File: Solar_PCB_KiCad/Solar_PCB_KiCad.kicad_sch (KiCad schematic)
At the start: 1 part, among them U1 LT3652EMSE

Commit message: Updated Schematic
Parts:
- added C1, C2: C, symbol Device:C
- added D1, D2: LED, symbol Device:LED
- added D3, D4: D_Schottky, symbol Device:D_Schottky
- added J1, J2: Screw_Terminal_01x02, symbol Connector:Screw_Terminal_01x02
- added L1: L, symbol Device:L
- added R1, R2, R3, R4, R5, R6: R, symbol Device:R
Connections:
- net at U1.1 (V_{IN}): now also U1.2 (V_{IN_REG}), U1.3 (~{SHDN}), J1.1 (Pin_1), R1.1, R2.1
- net at U1.10 (SENSE): now also L1.2, R6.2
- net at U1.11 (BOOST): now also C2.2, D3.1 (K)
- net at U1.12 (SW): now also C2.1, D4.1 (K), L1.1
- net GND: now reaches U1.13 (GND)
- net GND: now also U1.6 (TIMER), C1.2, D4.2 (A), J1.2 (Pin_2), R4.1
- net at U1.4 (~{CHRG}): now also D1.1 (K)
- net at U1.5 (~{FAULT}): now also D2.1 (K)
- net at U1.7 (V_{FB}): now also R3.1
- net at U1.9 (BAT): now also C1.1, D3.2 (A), J2.1 (Pin_1), R5.1, R6.1
- new net: R3.2, R4.2, R5.2
- new net: D2.2 (A), R2.2
- new net: D1.2 (A), R1.2

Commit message: Updated schematic & PCB
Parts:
- C1, C2: footprint (none) -> Capacitor_SMD:C_0603_1608Metric
- D1, D2: footprint (none) -> LED_SMD:LED_0603_1608Metric
- D3, D4: footprint (none) -> Diode_SMD:D_0603_1608Metric
- J1, J2: footprint (none) -> TerminalBlock_Phoenix:TerminalBlock_Phoenix_MKDS-1,5-2-5.08_1x02_P5.08mm_Horizontal
- L1: footprint (none) -> Inductor_SMD:L_0603_1608Metric
- R1, R2, R3, R4, R5, R6: footprint (none) -> Resistor_SMD:R_0603_1608Metric
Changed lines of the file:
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@@
 			)
 		)
-		(property "Footprint" ""
+		(property "Footprint" "Diode_SMD:D_0603_1608Metric"
 			(at 175.26 80.01 0)
 			(effects
@@
 			)
 		)
-		(property "Footprint" ""
+		(property "Footprint" "Resistor_SMD:R_0603_1608Metric"
 			(at 198.12 90.678 90)
 			(effects
@@
 			)
 		)
-		(property "Footprint" ""
+		(property "Footprint" "Inductor_SMD:L_0603_1608Metric"
 			(at 186.69 88.9 0)
 			(effects
@@
 			)
 		)
-		(property "Footprint" ""
+		(property "Footprint" "Resistor_SMD:R_0603_1608Metric"
 			(at 179.832 113.03 90)
 			(effects
@@
 			)
 		)
-		(property "Footprint" ""
+		(property "Footprint" "TerminalBlock_Phoenix:TerminalBlock_Phoenix_MKDS-1,5-2-5.08_1x02_P5.08mm_Horizontal"
 			(at 102.87 77.47 0)
 			(effects
@@
 			)
 		)
-		(property "Footprint" ""
+		(property "Footprint" "Resistor_SMD:R_0603_1608Metric"
 			(at 127 103.632 90)
 			(effects
@@
 			)
 		)
-		(property "Footprint" ""
+		(property "Footprint" "Capacitor_SMD:C_0603_1608Metric"
 			(at 176.2252 96.52 0)
 			(effects
@@
 			)
 		)
-		(property "Footprint" ""
+		(property "Footprint" "LED_SMD:LED_0603_1608Metric"
 			(at 135.89 105.41 0)
 			(effects
@@
 			)
 		)
-		(property "Footprint" ""
+		(property "Footprint" "Capacitor_SMD:C_0603_1608Metric"
 			(at 199.0852 116.84 0)
 			(effects
@@
 			)
 		)
-		(property "Footprint" ""
+		(property "Footprint" "Resistor_SMD:R_0603_1608Metric"
 			(at 187.96 108.458 90)
 			(effects
@@
 			)
 		)
-		(property "Footprint" ""
+		(property "Footprint" "LED_SMD:LED_0603_1608Metric"
 			(at 135.89 100.33 0)
 			(effects
@@
 			)
 		)
-		(property "Footprint" ""
+		(property "Footprint" "TerminalBlock_Phoenix:TerminalBlock_Phoenix_MKDS-1,5-2-5.08_1x02_P5.08mm_Horizontal"
 			(at 227.33 88.9 0)
 			(effects
@@
 			)
 		)
-		(property "Footprint" ""
+		(property "Footprint" "Diode_SMD:D_0603_1608Metric"
 			(at 186.69 96.52 0)
 			(effects
@@
 			)
 		)
-		(property "Footprint" ""
+		(property "Footprint" "Resistor_SMD:R_0603_1608Metric"
 			(at 175.26 104.902 90)
 			(effects
@@
 			)
 		)
-		(property "Footprint" ""
+		(property "Footprint" "Resistor_SMD:R_0603_1608Metric"
 			(at 127 102.108 90)
 			(effects

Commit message: Updated Schematics
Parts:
- added C3: 10u, Capacitor_SMD:C_0603_1608Metric, symbol Device:C
- C1: value C -> 10u
- C2: value C -> 1u
- D1: value LED -> GREEN LED
- D2: value LED -> RED LED
- R1, R2: value R -> 2k
- R3: value R -> 67.2k
- R4: value R -> 330k
- R5: value R -> 410k
- R6: value R -> 0.2
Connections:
- net GND: now also C3.2
- net at J1.1 (Pin_1), R1.1, R2.1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: now also C3.1
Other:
- title: (none) -> Solar_PCB
- moved on the sheet: J1

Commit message: Updated simulation
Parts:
- added D5: D_Schottky, Diode_SMD:D_0603_1608Metric, symbol Device:D_Schottky
- L1: value L -> 18.91uH; footprint Inductor_SMD:L_0603_1608Metric -> Inductor_THT:L_Radial_D7.8mm_P5.00mm_Fastron_07HCP
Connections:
- net GND: now also J2.2 (Pin_2)
- net at C3.1, R1.1, R2.1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: now also D5.1 (K); no longer J1.1 (Pin_1)
- new net: D5.2 (A), J1.1 (Pin_1)
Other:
- moved on the sheet: C2, C3, D1, D2, D4, J1, J2, L1, R1, R2, R6

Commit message: Updated BOM
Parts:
- R1, R2: value 2k -> 100
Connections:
- net at C3.1, D5.1 (K), U1.1 (V_{IN})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: now also D1.2 (A), D2.2 (A); no longer R1.1, R2.1
- net at R2.2: now also U1.5 (~{FAULT}); no longer D2.2 (A)
- net at D2.1 (K): now also R2.1; no longer U1.5 (~{FAULT})
- net at D1.1 (K): now also R1.1; no longer U1.4 (~{CHRG})
- net at R1.2: now also U1.4 (~{CHRG}); no longer D1.2 (A)
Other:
- moved on the sheet: D1, D2, R1, R2
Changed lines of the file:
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@@
 		)
 	)
-	(text_box "Solar Panel Input\n12V 300mA 4W Max"
+	(text_box "Solar Panel Input\n12V 350mA 4W Max"
 		(exclude_from_sim no)
 		(at 45.72 88.9 0)
@@
 		)
 	)
-	(text_box "Status pins can sink up to 10mA\n\nI = 12V/2k = 6mA"
+	(text_box "Status pins can sink up to 10mA\n\nI = (12V-2V)/100 = 100mA"
 		(exclude_from_sim no)
 		(at 86.36 101.6 0)
@@
 	(symbol
 		(lib_id "Device:R")
-		(at 123.19 105.41 90)
+		(at 132.08 105.41 90)
 		(mirror x)
 		(unit 1)
@@
 		(dnp no)
 		(property "Reference" "R2"
-			(at 123.19 111.76 90)
-			(effects
-				(font
-					(size 1.27 1.27)
-				)
-			)
-		)
-		(property "Value" "2k"
-			(at 123.19 109.22 90)
+			(at 132.08 111.76 90)
+			(effects
+				(font
+					(size 1.27 1.27)
+				)
+			)
+		)
+		(property "Value" "100"
+			(at 132.08 109.22 90)
 			(effects
 				(font
@@
 		)
 		(property "Footprint" "Resistor_SMD:R_0603_1608Metric"
-			(at 123.19 103.632 90)
+			(at 132.08 103.632 90)
 			(effects
 				(font
@@
 		)
 		(property "Datasheet" "~"
-			(at 123.19 105.41 0)
+			(at 132.08 105.41 0)
 			(effects
 				(font
@@
 		)
 		(property "Description" "Resistor"
-			(at 123.19 105.41 0)
+			(at 132.08 105.41 0)
 			(effects
 				(font
@@
 	(symbol
 		(lib_id "Device:LED")
-		(at 132.08 105.41 0)
+		(at 123.19 105.41 0)
 		(mirror y)
 		(unit 1)
@@
 		(dnp no)
 		(property "Reference" "D2"
-			(at 133.6675 113.03 0)
+			(at 124.7775 113.03 0)
 			(effects
 				(font
@@
 		)
 		(property "Value" "RED LED"
-			(at 133.6675 110.49 0)
+			(at 124.7775 110.49 0)
 			(effects
 				(font
@@
 		)
 		(property "Footprint" "LED_SMD:LED_0603_1608Metric"
-			(at 132.08 105.41 0)
+			(at 123.19 105.41 0)
 			(effects
 				(font
@@
 		)
 		(property "Datasheet" "~"
-			(at 132.08 105.41 0)
+			(at 123.19 105.41 0)
 			(effects
 				(font
@@
 		)
 		(property "Description" "Light emitting diode"
-			(at 132.08 105.41 0)
+			(at 123.19 105.41 0)
 			(effects
 				(font
@@
 	(symbol
 		(lib_id "Device:LED")
-		(at 132.08 100.33 180)
+		(at 123.19 100.33 180)
 		(unit 1)
 		(exclude_from_sim no)
@@
 		(fields_autoplaced yes)
 		(property "Reference" "D1"
-			(at 133.6675 92.71 0)
+			(at 124.7775 92.71 0)
 			(effects
 				(font
@@
 		)
 		(property "Value" "GREEN LED"
-			(at 133.6675 95.25 0)
+			(at 124.7775 95.25 0)
 			(effects
 				(font
@@
 		)
 		(property "Footprint" "LED_SMD:LED_0603_1608Metric"
-			(at 132.08 100.33 0)
+			(at 123.19 100.33 0)
 			(effects
 				(font
@@
 		)
 		(property "Datasheet" "~"
-			(at 132.08 100.33 0)
+			(at 123.19 100.33 0)
 			(effects
 				(font
@@
 		)
 		(property "Description" "Light emitting diode"
-			(at 132.08 100.33 0)
+			(at 123.19 100.33 0)
 			(effects
 				(font
@@
 	(symbol
 		(lib_id "Device:R")
-		(at 123.19 100.33 90)
+		(at 132.08 100.33 90)
 		(unit 1)
 		(exclude_from_sim no)
@@
 		(fields_autoplaced yes)
 		(property "Reference" "R1"
-			(at 123.19 93.98 90)
-			(effects
-				(font
-					(size 1.27 1.27)
-				)
-			)
-		)
-		(property "Value" "2k"
-			(at 123.19 96.52 90)
+			(at 132.08 93.98 90)
+			(effects
+				(font
+					(size 1.27 1.27)
+				)
+			)
+		)
+		(property "Value" "100"
+			(at 132.08 96.52 90)
 			(effects
 				(font
@@
 		)
 		(property "Footprint" "Resistor_SMD:R_0603_1608Metric"
-			(at 123.19 102.108 90)
+			(at 132.08 102.108 90)
 			(effects
 				(font
@@
 		)
 		(property "Datasheet" "~"
-			(at 123.19 100.33 0)
+			(at 132.08 100.33 0)
 			(effects
 				(font
@@
 		)
 		(property "Description" "Resistor"
-			(at 123.19 100.33 0)
-			(effects
-				(font
+			(at 132.08 100.33 0)
+			(effects
+				(font

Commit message: Updated KiCad
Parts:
- added C4: 1u, Capacitor_SMD:C_0603_1608Metric, symbol Device:C
- added J3: Screw_Terminal_01x02, TerminalBlock_Phoenix:TerminalBlock_Phoenix_MKDS-1,5-2-5.08_1x02_P5.08mm_Horizontal, symbol Connector:Screw_Terminal_01x02
- added R7: 270k, Resistor_SMD:R_0603_1608Metric, symbol Device:R
- added R8: 100k, Resistor_SMD:R_0603_1608Metric, symbol Device:R
- D3, D5: footprint Diode_SMD:D_0603_1608Metric -> Diode_SMD:D_SOD-323
- L1: value 18.91uH -> 20uH
- R1, R2: value 100 -> 1k
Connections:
- net GND: now also C4.2, J3.2 (Pin_2), R8.1
- net at C1.1, D3.2 (A), J2.1 (Pin_1)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: now also J3.1 (Pin_1)
- net at C3.1, D1.2 (A), D2.2 (A)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: now also C4.1, R7.2; no longer U1.2 (V_{IN_REG})
- new net: R7.1, R8.2, U1.2 (V_{IN_REG})
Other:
- moved on the sheet: C3, D5, J1, J2

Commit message: Updated BOM
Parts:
- R1, R2: value 1k -> 1.1k
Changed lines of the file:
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@@
 			)
 		)
-		(property "Value" "1k"
+		(property "Value" "1.1k"
 			(at 132.08 109.22 90)
 			(effects
@@
 			)
 		)
-		(property "Value" "1k"
+		(property "Value" "1.1k"
 			(at 132.08 96.52 90)
 			(effects

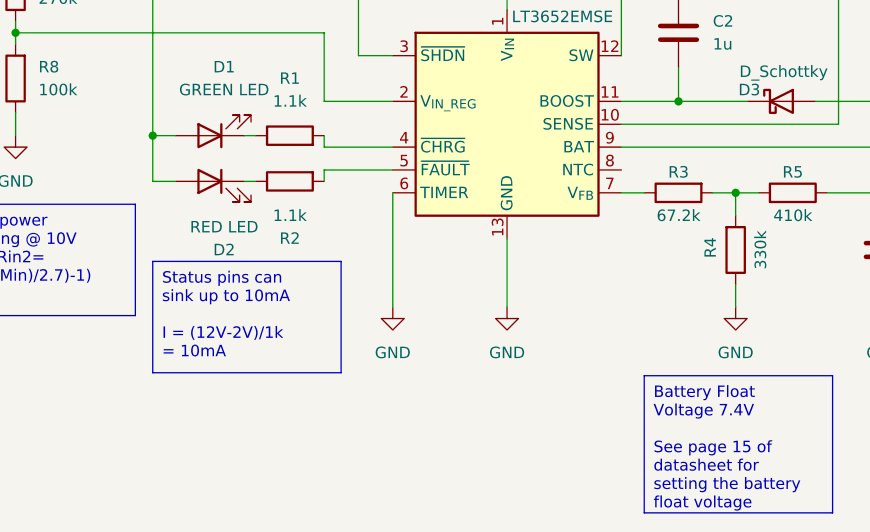
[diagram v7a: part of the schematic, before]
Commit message: Updated Datasheets
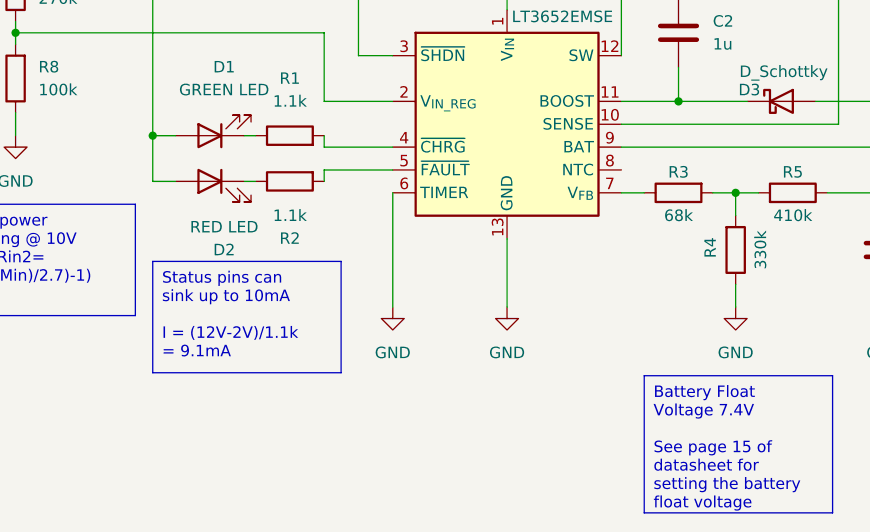
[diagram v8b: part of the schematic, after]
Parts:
- D4: footprint Diode_SMD:D_0603_1608Metric -> Diode_SMD:D_SMC
- R3: value 67.2k -> 68k
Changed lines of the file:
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@@
 		)
 	)
-	(text_box "Status pins can sink up to 10mA\n\nI = (12V-2V)/1k = 10mA"
+	(text_box "Status pins can sink up to 10mA\n\nI = (12V-2V)/1.1k = 9.1mA"
 		(exclude_from_sim no)
 		(at 116.84 114.3 0)
@@
 			)
 		)
-		(property "Footprint" "Diode_SMD:D_0603_1608Metric"
+		(property "Footprint" "Diode_SMD:D_SMC"
 			(at 175.26 71.12 0)
 			(effects
@@
 			)
 		)
-		(property "Datasheet" "~"
+		(property "Datasheet" "https://www.onsemi.com/pdf/datasheet/mbrs340t3-d.pdf"
 			(at 175.26 71.12 0)
 			(effects
@@
 			)
 		)
-		(property "Datasheet" "~"
+		(property "Datasheet" "https://mm.digikey.com/Volume0/opasdata/d220001/medias/docus/609/CL10A105KA8NNNC_Spec.pdf"
 			(at 129.54 71.12 0)
 			(effects
@@
 			)
 		)
-		(property "Datasheet" "~"
+		(property "Datasheet" "https://www.bourns.com/docs/Product-Datasheets/CRL.pdf"
 			(at 198.12 81.28 0)
 			(effects
@@
 			)
 		)
-		(property "Datasheet" "~"
+		(property "Datasheet" "https://mm.digikey.com/Volume0/opasdata/d220001/medias/docus/666/744772200.pdf"
 			(at 186.69 81.28 0)
 			(effects
@@
 			)
 		)
-		(property "Datasheet" "~"
+		(property "Datasheet" "https://industrial.panasonic.com/cdbs/www-data/pdf/RDA0000/AOA0000C304.pdf"
 			(at 181.61 113.03 0)
 			(effects
@@
 			)
 		)
-		(property "Datasheet" "~"
+		(property "Datasheet" "https://industrial.panasonic.com/cdbs/www-data/pdf/RDA0000/AOA0000C304.pdf"
 			(at 132.08 105.41 0)
 			(effects
@@
 			)
 		)
-		(property "Datasheet" "~"
+		(property "Datasheet" "https://industrial.panasonic.com/cdbs/www-data/pdf/RDA0000/AOA0000C304.pdf"
 			(at 101.6 83.82 0)
 			(effects
@@
 			)
 		)
-		(property "Datasheet" "~"
+		(property "Datasheet" "https://mm.digikey.com/Volume0/opasdata/d220001/medias/docus/609/CL10A105KA8NNNC_Spec.pdf"
 			(at 175.26 88.9 0)
 			(effects
@@
 			)
 		)
-		(property "Datasheet" "~"
+		(property "Datasheet" "https://www.we-online.com/components/products/datasheet/150060VS75000.pdf"
 			(at 123.19 105.41 0)
 			(effects
@@
 			)
 		)
-		(property "Datasheet" "~"
+		(property "Datasheet" "https://mm.digikey.com/Volume0/opasdata/d220001/medias/docus/658/CL10A106MA8NRNC_Spec.pdf"
 			(at 90.17 83.82 0)
 			(effects
@@
 			)
 		)
-		(property "Datasheet" "~"
+		(property "Datasheet" "https://mm.digikey.com/Volume0/opasdata/d220001/medias/docus/658/CL10A106MA8NRNC_Spec.pdf"
 			(at 198.12 113.03 0)
 			(effects
@@
 			)
 		)
-		(property "Datasheet" "~"
+		(property "Datasheet" "https://www.yageo.com/upload/media/product/products/datasheet/rchip/PYu-RC_Group_51_RoHS_L_12.pdf"
 			(at 187.96 106.68 0)
 			(effects
@@
 			)
 		)
-		(property "Datasheet" "~"
+		(property "Datasheet" "https://www.we-online.com/components/products/datasheet/150060VS75000.pdf"
 			(at 123.19 100.33 0)
 			(effects
@@
 			)
 		)
-		(property "Datasheet" "~"
+		(property "Datasheet" "https://www.mccsemi.com/pdf/Products/B5817WS-B5819WS(SOD-323).PDF"
 			(at 82.55 77.47 0)
 			(effects
@@
 			)
 		)
-		(property "Datasheet" "~"
+		(property "Datasheet" "https://www.digikey.ca/en/products/detail/panasonic-electronic-components/ERJ-3EKF1003V/196075"
 			(at 101.6 93.98 0)
 			(effects
@@
 			)
 		)
-		(property "Datasheet" "~"
+		(property "Datasheet" "https://www.mccsemi.com/pdf/Products/B5817WS-B5819WS(SOD-323).PDF"
 			(at 186.69 96.52 0)
 			(effects
@@
 			)
 		)
-		(property "Value" "67.2k"
+		(property "Value" "68k"
 			(at 175.26 109.22 90)
 			(effects
@@
 			)
 		)
-		(property "Datasheet" "~"
+		(property "Datasheet" "https://industrial.panasonic.com/cdbs/www-data/pdf/RDA0000/AOA0000C304.pdf"
 			(at 175.26 106.68 0)
 			(effects
@@
 			)
 		)
-		(property "Datasheet" "~"
+		(property "Datasheet" "https://industrial.panasonic.com/cdbs/www-data/pdf/RDA0000/AOA0000C304.pdf"
 			(at 132.08 100.33 0)
 			(effects
